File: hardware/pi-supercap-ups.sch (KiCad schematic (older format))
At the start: 5 parts, among them J1 Screw_Terminal_01x04, J2 Raspberry_Pi_2_3

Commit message: Implement next hardware revision
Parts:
- added C1: 47uF, Capacitor_SMD:C_0805_2012Metric_Pad1.15x1.40mm_HandSolder, symbol Device:C
- added D1: SMF16CA, Diode_SMD:D_SOD-123F, symbol Device:D_TVS
- added D2: DS34W, Diode_SMD:D_SOD-123F, symbol Diode:1N5820
- added D3, D4, D5: RLED, Diode_SMD:D_0603_1608Metric_Pad1.05x0.95mm_HandSolder, symbol Device:LED
- added F1: 1A, Fuse:Fuse_1206_3216Metric_Pad1.42x1.75mm_HandSolder, symbol Device:Fuse
- added J3: Conn_01x08_Male, Connector_PinHeader_2.54mm:PinHeader_1x08_P2.54mm_Vertical, symbol Connector:Conn_01x08_Male
- added J4: Conn_01x02_Male, Connector_PinHeader_2.54mm:PinHeader_1x02_P2.54mm_Vertical, symbol Connector:Conn_01x02_Male
- added JP2, JP3, JP4, JP5, JP6: SolderJumper_2_Open, custom:SolderJumper-2_P1.3mm_OpenMask_RoundedPad1.0x1.5mm, symbol Jumper:SolderJumper_2_Open
- added JP7: SolderJumper_3_Open, custom:SolderJumper-3_P1.3mm_OpenMask_RoundedPad1.0x1.5mm, symbol Jumper:SolderJumper_3_Open
- added R1: 4.7k, Resistor_SMD:R_0603_1608Metric_Pad1.05x0.95mm_HandSolder, symbol Device:R
- added R2, R20, R21, R3: 2.2k, Resistor_SMD:R_0603_1608Metric_Pad1.05x0.95mm_HandSolder, symbol Device:R
- added TP1: +12V_prot, TestPoint:TestPoint_Keystone_5000-5004_Miniature, symbol Connector:TestPoint
- J1: footprint TerminalBlock_MetzConnect:TerminalBlock_MetzConnect_Type055_RT01504HDWU_1x04_P5.00mm_Horizontal -> custom:15EDGVC-3.81-4P
- R4: renamed from R1; value 680R -> 1.5k
- renumbered D1 to D6, TP1 to TP2
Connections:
- net +12V: now also F1.2
- net 3.3V: now also J3.8 (Pin_8)
- net 5V: now also C1.1, R20.1, R3.1
- net ATSCK: now also J3.7 (Pin_7), JP3.1 (A); no longer J2.40 (GPIO21/SCLK1)
- net ATTiny_RESET: now also J3.1 (Pin_1), JP2.1 (A); no longer J2.36 (GPIO16)
- net GND: now also C1.2, D1.2 (A2), D3.1 (K), D4.1 (K), D5.1 (K), J3.4 (Pin_4), R21.2
- net GPIO3: now also JP6.2 (B)
- net MISO: now also J3.6 (Pin_6), JP4.1 (A); no longer J2.35 (GPIO19/MISO1)
- net Sense_Vcc: now also J4.1 (Pin_1), JP7.2 (C); no longer J2.37 (GPIO26)
- net inv_Sense_EN renamed GPIO20
- net GPIO20: now also JP5.2 (B)
- new net: D4.2 (A), R2.2
- new net: D5.2 (A), R3.2
- new net: D3.2 (A), R1.2
- new net 12V_fused: D1.1 (A1), D2.2 (A), F1.1
- new net 2.5V: J4.2 (Pin_2), R20.2, R21.1
- new net Boost converter/Vin: R2.1
- new net Buck converter/Vin: D2.1 (K), R1.1, TP1.1
- new net GPIO16: J2.36 (GPIO16), JP2.2 (B)
- new net GPIO19: J2.35 (GPIO19/MISO1), JP4.2 (B)
- new net GPIO21: J2.40 (GPIO21/SCLK1), JP3.2 (B)
- new net GPIO26: J2.37 (GPIO26), JP7.3 (B)
- new net MOSI: J3.5 (Pin_5), JP5.1 (A)
- new net PB3: J3.2 (Pin_2), JP7.1 (A)
- new net PB4: J3.3 (Pin_3), JP6.1 (A)
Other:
- note added: "Sense_Vcc"
- note added: "inv_Sense_EN"
- moved on the sheet: D6, J1, J2, R4, TP2

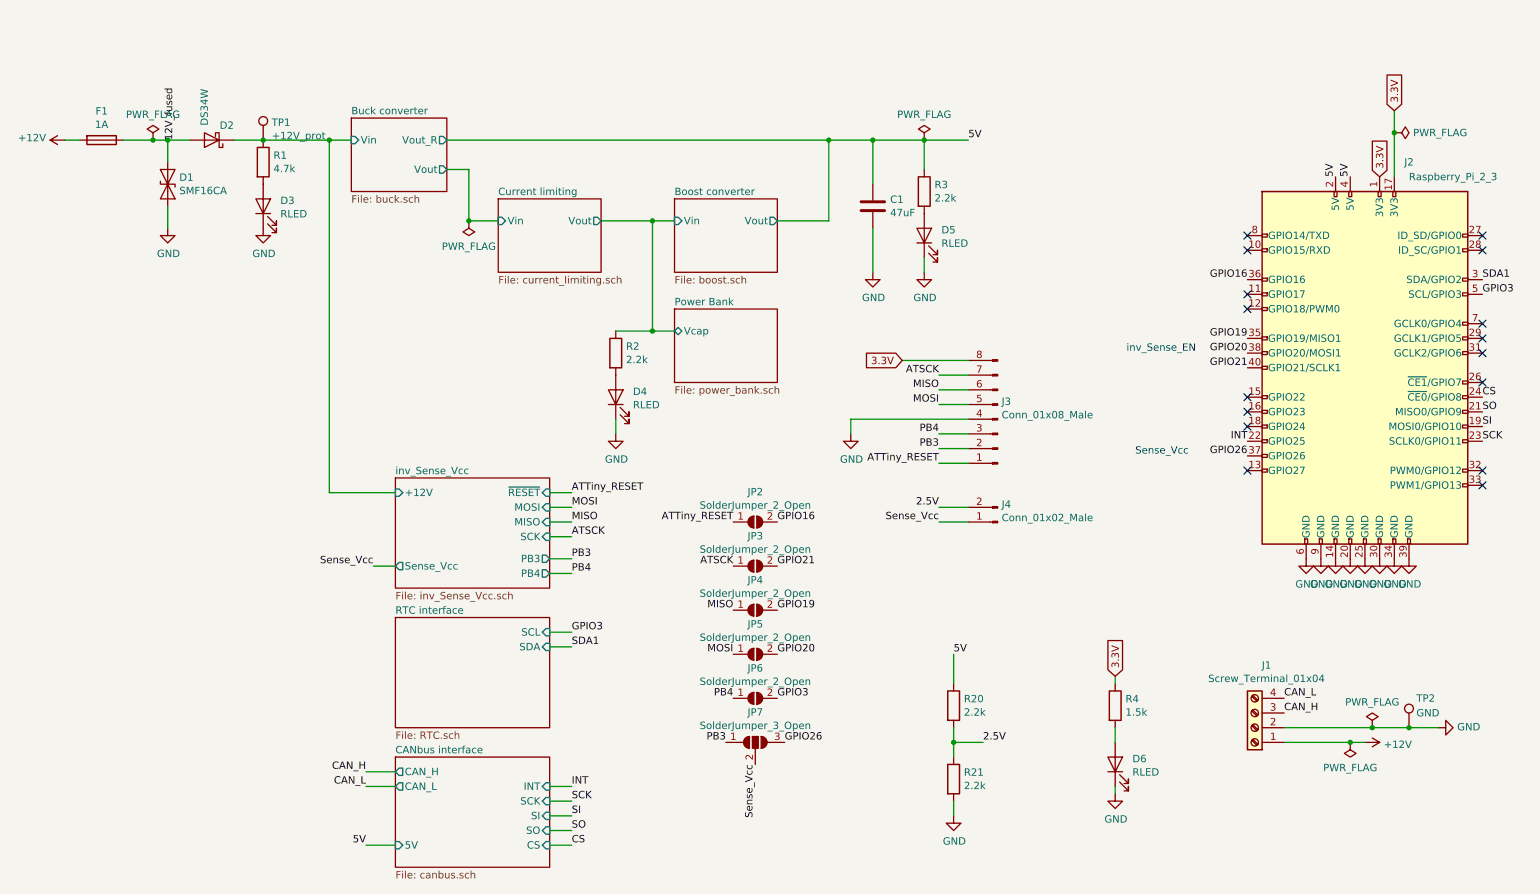
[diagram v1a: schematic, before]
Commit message: Changed to pure-serial topology. Changed to beefier mcu.
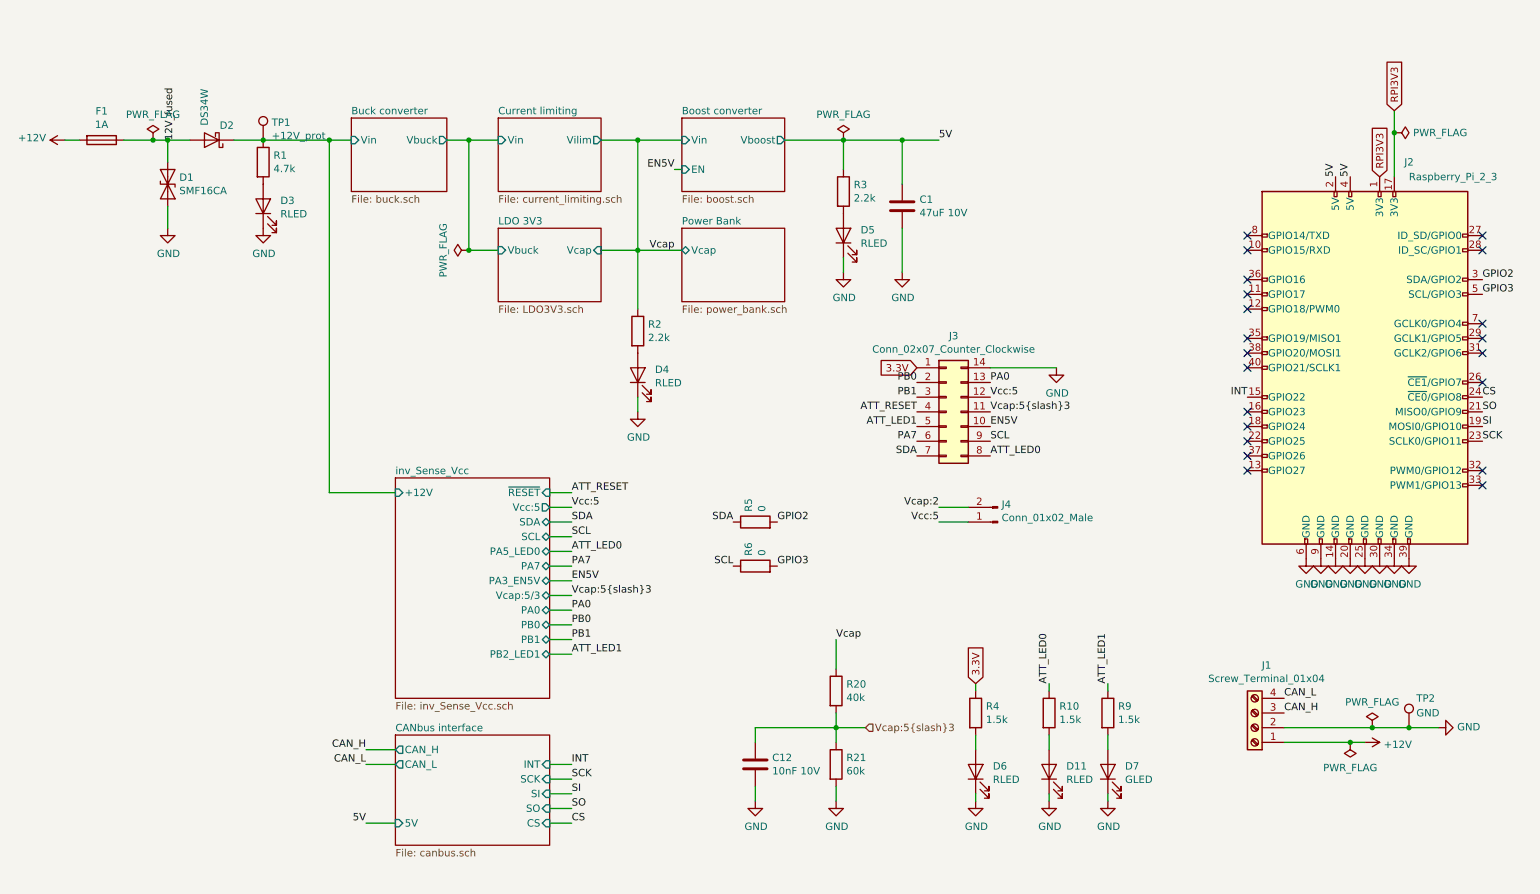
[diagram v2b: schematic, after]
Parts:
- removed J3: Conn_01x08_Male, Connector_PinHeader_2.54mm:PinHeader_1x08_P2.54mm_Vertical, symbol Connector:Conn_01x08_Male
- removed JP2, JP3, JP4, JP5, JP6: SolderJumper_2_Open, custom:SolderJumper-2_P1.3mm_OpenMask_RoundedPad1.0x1.5mm, symbol Jumper:SolderJumper_2_Open
- removed JP7: SolderJumper_3_Open, custom:SolderJumper-3_P1.3mm_OpenMask_RoundedPad1.0x1.5mm, symbol Jumper:SolderJumper_3_Open
- added C12: 10nF 10V, Capacitor_SMD:C_0603_1608Metric_Pad1.05x0.95mm_HandSolder, symbol Device:C
- added D11: RLED, LED_SMD:LED_0603_1608Metric_Pad1.05x0.95mm_HandSolder, symbol Device:LED
- added D7: GLED, LED_SMD:LED_0603_1608Metric_Pad1.05x0.95mm_HandSolder, symbol Device:LED
- added J3: Conn_02x07_Counter_Clockwise, symbol Connector_Generic:Conn_02x07_Counter_Clockwise
- added R10, R9: 1.5k, Resistor_SMD:R_0603_1608Metric_Pad1.05x0.95mm_HandSolder, symbol Device:R
- added R5, R6: 0, Resistor_SMD:R_0603_1608Metric_Pad1.05x0.95mm_HandSolder, symbol Device:R
- C1: value 47uF -> 47uF 10V
- R20: value 2.2k -> 40k
- R21: value 2.2k -> 60k
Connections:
- net 3.3V: now also J3.1 (Pin_1); no longer J2.1 (3V3), J2.17 (3V3)
- net 5V: no longer R20.1
- net GND: now also C12.2, D11.1 (K), D7.1 (K), J3.14 (Pin_14)
- net GPIO3: now also R6.2
- net INT: now also J2.15 (GPIO22); no longer J2.22 (GPIO25)
- net 2.5V renamed Vcap:5/3
- net Vcap:5/3: now also C12.1, J3.11 (Pin_11); no longer J4.2 (Pin_2)
- net Boost converter/Vin renamed Vcap
- net Vcap: now also R20.1
- net GPIO16: no longer names the net of J2.36 (GPIO16)
- net GPIO19: no longer names the net of J2.35 (GPIO19/MISO1)
- net GPIO20: no longer names the net of J2.38 (GPIO20/MOSI1)
- net GPIO21: no longer names the net of J2.40 (GPIO21/SCLK1)
- net GPIO26: no longer names the net of J2.37 (GPIO26)
- net SDA1 renamed GPIO2
- net GPIO2: now also R5.2
- net Sense_Vcc renamed Vcc:5
- net Vcc:5: now also J3.12 (Pin_12)
- new net: D11.2 (A), R10.2
- new net: D7.2 (A), R9.2
- new net ATT_LED0: J3.8 (Pin_8), R10.1
- new net ATT_LED1: J3.5 (Pin_5), R9.1
- new net ATT_RESET: J3.4 (Pin_4)
- new net EN5V: J3.10 (Pin_10)
- new net PA0: J3.13 (Pin_13)
- new net PA7: J3.6 (Pin_6)
- new net PB0: J3.2 (Pin_2)
- new net PB1: J3.3 (Pin_3)
- new net RPI3V3: J2.1 (3V3), J2.17 (3V3)
- new net SCL: J3.9 (Pin_9), R6.1
- new net SDA: J3.7 (Pin_7), R5.1
- new net Vcap:2: J4.2 (Pin_2)
- no-connect marks 16 -> 21
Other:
- note removed: "Sense_Vcc"
- note removed: "inv_Sense_EN"
- moved on the sheet: C1, D4, D5, D6, R2, R20, R21, R3, R4

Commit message: Layout partially done before change of plans
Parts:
- removed D4: RLED, Diode_SMD:D_0603_1608Metric_Pad1.05x0.95mm_HandSolder, symbol Device:LED
- removed D6: RLED, LED_SMD:LED_0603_1608Metric_Pad1.05x0.95mm_HandSolder, symbol Device:LED
- removed R2: 2.2k, Resistor_SMD:R_0603_1608Metric_Pad1.05x0.95mm_HandSolder, symbol Device:R
- removed R21: 60k, Resistor_SMD:R_0603_1608Metric_Pad1.05x0.95mm_HandSolder, symbol Device:R
- removed R4: 1.5k, Resistor_SMD:R_0603_1608Metric_Pad1.05x0.95mm_HandSolder, symbol Device:R
- added TP3: Vcap, TestPoint:TestPoint_Keystone_5000-5004_Miniature, symbol Connector:TestPoint
- C12: value 10nF 10V -> 10nF 5V
- J1: footprint custom:15EDGVC-3.81-4P -> custom:WJ2EDGR-5.08-4P
- J3: footprint (none) -> custom:PinHeader_2x07_P2.54mm_Vertical_CounterClockwise
- J4: footprint Connector_PinHeader_2.54mm:PinHeader_1x02_P2.54mm_Vertical -> custom:WJ2EDGR-5.08-2P
- R20: value 40k -> 100k
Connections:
- net PB1 is gone; now on net ATT_LED0: J3.3 (Pin_3)
- net RPI3V3 is gone; now on net 3.3V: J2.1 (3V3), J2.17 (3V3)
- net Vcap:2 is gone; now on net Vcap: J4.2 (Pin_2)
- net 3.3V: no longer J3.1 (Pin_1)
- net ATT_LED0: no longer J3.8 (Pin_8)
- net GND: now also J4.1 (Pin_1)
- net Vcap: now also TP3.1
- net Vcap:5/3 renamed VcapS
- net Vcc:5 renamed V12:6
- net V12:6: no longer J4.1 (Pin_1)
- new net ATT_Vcc: J3.1 (Pin_1)
- new net PA5: J3.8 (Pin_8)
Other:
- note added: "Pins SDA, SCL, and PA5 are used for reflashing"
- note added: "Supercaps are now behind a separate connector (min. 8A)"
- moved on the sheet: C12

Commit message: revE ready for production
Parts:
- removed J4: Conn_01x02_Male, custom:WJ2EDGR-5.08-2P, symbol Connector:Conn_01x02_Male
- added J4: Screw_Terminal_01x02, custom:TerminalBlock_WJ15EDGRC-3.81-2P, symbol Connector:Screw_Terminal_01x02
- added J5: Screw_Terminal_01x03, custom:TerminalBlock_WJ15EDGRC-3.81-3P, symbol Connector:Screw_Terminal_01x03
- added R4, R8: 0, Resistor_SMD:R_0603_1608Metric_Pad1.05x0.95mm_HandSolder, symbol Device:R
- C12: value 10nF 5V -> 100nF
- D3, D5: footprint Diode_SMD:D_0603_1608Metric_Pad1.05x0.95mm_HandSolder -> LED_SMD:LED_0603_1608Metric_Pad1.05x0.95mm_HandSolder
- J1: footprint custom:WJ2EDGR-5.08-4P -> custom:TerminalBlock_WJ15EDGRC-3.81-4P
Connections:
- net +12V: now also J1.2 (Pin_2); no longer J1.1 (Pin_1)
- net GND: now also J1.1 (Pin_1), J4.1 (Pin_1), J5.1 (Pin_1); no longer J1.2 (Pin_2)
- net Vcap: now also J4.2 (Pin_2)
- net GPIO27: now reaches J2.13 (GPIO27)
- net GPIO27: now also R8.2
- net CS1: now reaches J2.26 (~CE1~/GPIO7)
- net CAN_H renamed CAN0_L
- net CAN_L renamed CAN0_H
- net CS renamed CS0
- net INT renamed GPIO22
- net GPIO22: now also R4.2
- new net CAN1_H: J5.3 (Pin_3)
- new net CAN1_L: J5.2 (Pin_2)
- new net INT0: R4.1
- new net INT1: R8.1
- no-connect marks 21 -> 19
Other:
- note added: "0R resistors allow for disabling or re-routing\nsignals connected to Raspi GPIOs"
- moved on the sheet: C12, J1, J3, R20, R5, R6, TP2

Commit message: Add ENIN trace to the PCB. Change input voltage dividers for 1.1V ref.
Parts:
- removed C12: 100nF, Capacitor_SMD:C_0603_1608Metric_Pad1.05x0.95mm_HandSolder, symbol Device:C
- added R26: 68k, Resistor_SMD:R_0603_1608Metric_Pad1.05x0.95mm_HandSolder, symbol Device:R
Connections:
- net GND: now also R26.2
- net VcapS: now also R26.1
- net PA7 renamed ENIN
- net V12:6 renamed V12s
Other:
- note added: "VcapS is scaled from 2.7V to 1.1V"
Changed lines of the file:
@@
 	7900 2900 7550 2900
 NoConn ~ 10500 3650
-$Comp
-L power:PWR_FLAG #FLG0101
-U 1 1 5CF2FDF8
-P 3600 1650
-F 0 "#FLG0101" H 3600 1725 50  0001 C CNN
-F 1 "PWR_FLAG" H 3600 1824 50  0000 C CNN
-F 2 "" H 3600 1650 50  0001 C CNN
-F 3 "~" H 3600 1650 50  0001 C CNN
-	1    3600 1650
-	-1   0    0    1
-$EndComp
 Wire Wire Line
 	4750 1300 4750 2050
@@
 F2 "+12V" I L 3100 2800 50
 F3 "~RESET~" I R 4150 2800 50
-F4 "V12:6" O R 4150 2900 50
+F4 "V12s" O R 4150 2900 50
 F5 "SDA" B R 4150 3000 50
 F6 "SCL" B R 4150 3100 50
 F7 "PA5" B R 4150 3200 50
-F8 "PA7" B R 4150 3300 50
+F8 "PA7_ENIN" B R 4150 3300 50
 F9 "PA3_EN5V" B R 4150 3400 50
 F10 "PA0" B R 4150 3600 50
@@
 EN5V
 Text Label 4300 3300 0    50   ~ 0
-PA7
+ENIN
 Text Label 4300 3100 0    50   ~ 0
 SCL
@@
 SDA
 Text Label 4300 2900 0    50   ~ 0
-V12:6
+V12s
 Text Label 4300 3900 0    50   ~ 0
 ATT_LED1
@@
 	4150 3900 4300 3900
 Text Label 7550 3100 0    50   ~ 0
-V12:6
+V12s
 $Comp
 L power:GND #PWR0102
@@
 ATT_LED0
 Text Label 7050 3400 2    50   ~ 0
-PA7
+ENIN
 Text Label 7050 3500 2    50   ~ 0
 SDA
-$Comp
-L Device:C C12
-U 1 1 5D53C242
-P 6550 5550
-F 0 "C12" H 6665 5596 50  0000 L CNN
-F 1 "100nF" H 6665 5505 50  0000 L CNN
-F 2 "Capacitor_SMD:C_0603_1608Metric_Pad1.05x0.95mm_HandSolder" H 6588 5400 50  0001 C CNN
-F 3 "~" H 6550 5550 50  0001 C CNN
-	1    6550 5550
-	1    0    0    -1
-$EndComp
 $Comp
 L power:GND #PWR0105
@@
 F2 "Vin" I L 3800 1300 50
 F3 "Vilim" O R 4500 1300 50
+F4 "ENIN" I L 3800 1500 50
 $EndSheet
 Wire Wire Line
@@
 F2 "Vin" I L 2800 1300 50
 F3 "Vbuck" O R 3450 1300 50
+F4 "ENIN" I R 3450 1500 50
 $EndSheet
 Wire Wire Line
@@
 Connection ~ 3600 1300
 Connection ~ 4750 1300
-Wire Wire Line
-	3600 1300 3600 1650
 Wire Wire Line
 	5750 1300 6150 1300
@@
 NoConn ~ 8900 2250
 NoConn ~ 8900 3450
-Text GLabel 3600 1000 1    50   Input ~ 0
+Text GLabel 3600 800  1    50   Input ~ 0
 2.65V
 Wire Wire Line
-	3600 1000 3600 1300
+	3600 800  3600 900
 Text Label 2950 2950 2    50   ~ 0
 ATT_Vcc
@@
 Text GLabel 9800 1400 1    50   Input ~ 0
 3.3V
+$Comp
+L Device:R R26
+U 1 1 5DB5AEA1
+P 6550 5550
+F 0 "R26" H 6620 5596 50  0000 L CNN
+F 1 "68k" H 6620 5505 50  0000 L CNN
+F 2 "Resistor_SMD:R_0603_1608Metric_Pad1.05x0.95mm_HandSolder" V 6480 5550 50  0001 C CNN
+F 3 "~" H 6550 5550 50  0001 C CNN
+	1    6550 5550
+	1    0    0    -1
+$EndComp
+Text Notes 5100 5300 0    50   ~ 0
+VcapS is scaled from 2.7V to 1.1V
+Connection ~ 3600 900
+Wire Wire Line
+	3600 900  3600 1300
+$Comp
+L power:PWR_FLAG #FLG0101
+U 1 1 5CF2FDF8
+P 3600 900
+F 0 "#FLG0101" H 3600 975 50  0001 C CNN
+F 1 "PWR_FLAG" V 3600 1200 50  0000 C CNN
+F 2 "" H 3600 900 50  0001 C CNN
+F 3 "~" H 3600 900 50  0001 C CNN
+	1    3600 900
+	0    -1   -1   0
+$EndComp
+Wire Wire Line
+	3450 1500 3650 1500
+Wire Wire Line
+	3650 1500 3650 1950
+Connection ~ 3650 1500
+Wire Wire Line
+	3650 1500 3800 1500
+Text Label 3650 1950 0    50   ~ 0
+ENIN
 $EndSCHEMATC

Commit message: Fix component values etc
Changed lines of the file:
@@
 F2 "Vin" I L 2800 1300 50
 F3 "Vbuck" O R 3450 1300 50
-F4 "ENIN" I R 3450 1500 50
 $EndSheet
 Wire Wire Line
@@
 $EndComp
 Wire Wire Line
-	3450 1500 3650 1500
-Wire Wire Line
 	3650 1500 3650 1950
-Connection ~ 3650 1500
 Wire Wire Line
 	3650 1500 3800 1500
